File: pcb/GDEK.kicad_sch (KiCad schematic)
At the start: 326 parts, among them J1 TYPE-C-31-M-13C, J101 TYPE-C-31-M-13C, J102 AudioJack4, J103 Debug pads, J2 AudioJack4, J3 Debug pads, SW1 SW_Push_45deg, SW10 SW_Push_45deg, SW101 SW_Push_45deg, SW102 SW_Push_45deg, SW103 SW_Push_45deg, SW104 SW_Push_45deg, SW105 SW_Push_45deg, SW106 SW_Push_45deg, SW107 SW_Push_45deg, SW108 SW_Push_45deg, SW109 SW_Push_45deg, SW11 SW_Push_45deg, SW110 SW_Push_45deg, SW111 SW_Push_45deg, SW112 SW_Push_45deg, SW113 SW_Push_45deg, SW114 SW_Push_45deg, SW115 SW_Push_45deg, SW116 SW_Push_45deg, SW117 SW_Push_45deg, SW118 SW_Push_45deg, SW119 SW_Push_45deg, SW12 SW_Push_45deg, SW120 SW_Push_45deg, SW121 SW_Push_45deg, SW122 SW_Push_45deg, SW123 SW_Push_45deg, SW124 SW_Push_45deg, SW125 SW_Push_45deg, SW126 SW_Push_45deg, SW127 SW_Push_45deg, SW128 SW_Push_45deg, SW129 SW_Push_45deg, SW13 SW_Push_45deg, SW130 SW_Push_45deg, SW131 RotaryEncoder_Switch, SW14 SW_Push_45deg, SW15 SW_Push_45deg, SW16 SW_Push_45deg, SW17 SW_Push_45deg, SW18 SW_Push_45deg, SW19 SW_Push_45deg, SW2 SW_Push_45deg, SW20 SW_Push_45deg, SW21 SW_Push_45deg, SW22 SW_Push_45deg, SW23 SW_Push_45deg, SW24 SW_Push_45deg, SW25 SW_Push_45deg, SW26 SW_Push_45deg, SW27 SW_Push_45deg, SW28 SW_Push_45deg, SW29 SW_Push_45deg, SW3 SW_Push_45deg, SW30 SW_Push_45deg, SW31 RotaryEncoder_Switch, SW4 SW_Push_45deg, SW5 SW_Push_45deg, SW6 SW_Push_45deg, SW7 SW_Push_45deg, SW8 SW_Push_45deg, SW9 SW_Push_45deg, U1 RP2040, U101 RP2040, U102 W25Q128JVS, U103 74AHCT1G125, U104 USBLC6-2P6, U105 XC6210B332MR, U2 W25Q128JVS, U3 74AHCT1G125, U4 USBLC6-2P6, U5 XC6210B332MR, Y1 ABM8-272-T3, Y101 ABM8-272-T3

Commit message: ⚰️ Remove debug pins
YOLO.
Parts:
- removed J103, J3: Debug pads, Connector_PinHeader_2.54mm:PinHeader_1x04_P2.54mm_Vertical, symbol Connector:Conn_01x04_Socket
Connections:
- net ROW1: now also U1.31 (GPIO20); no longer U1.32 (GPIO21)
- net ROW2: now also U1.30 (GPIO19); no longer U1.31 (GPIO20)
- net ROW3: now also U1.29 (GPIO18); no longer U1.30 (GPIO19)
- net ROW4: now also U1.28 (GPIO17); no longer U1.29 (GPIO18)
- net at R102.1: now also U101.32 (GPIO21); no longer U101.41 (GPIO29_ADC3)
- net at R2.1: now also U1.32 (GPIO21); no longer U1.15 (GPIO12)
- no-connect marks 32 -> 36
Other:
- moved on the sheet: C116, C16, R102, R103, R104, R2, R3, R4, TP102, TP2, U102, U2

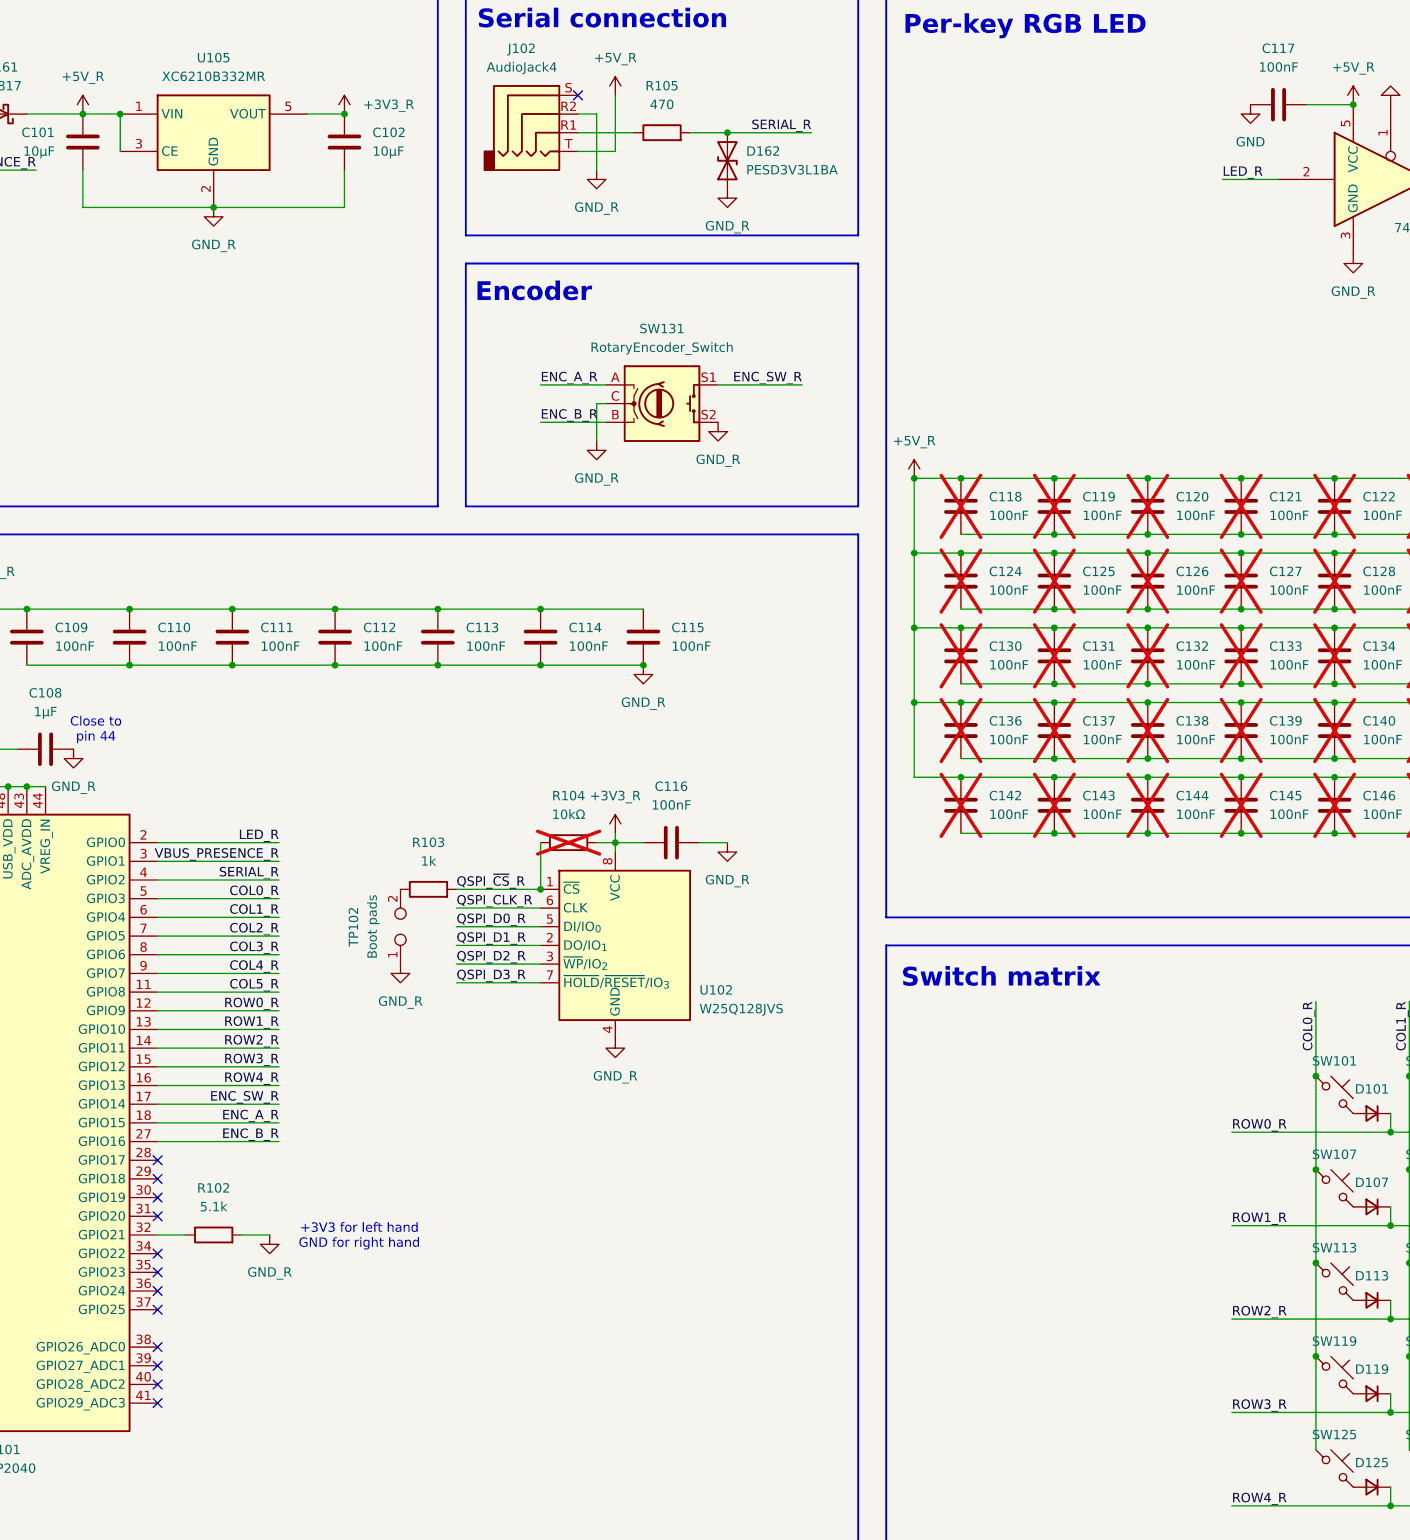
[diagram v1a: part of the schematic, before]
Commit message: ✨ Route right hand (except encoder)
Getting late! Will hopefully finish tomorrow. Then DRC, then panelization with vcuts, then order!
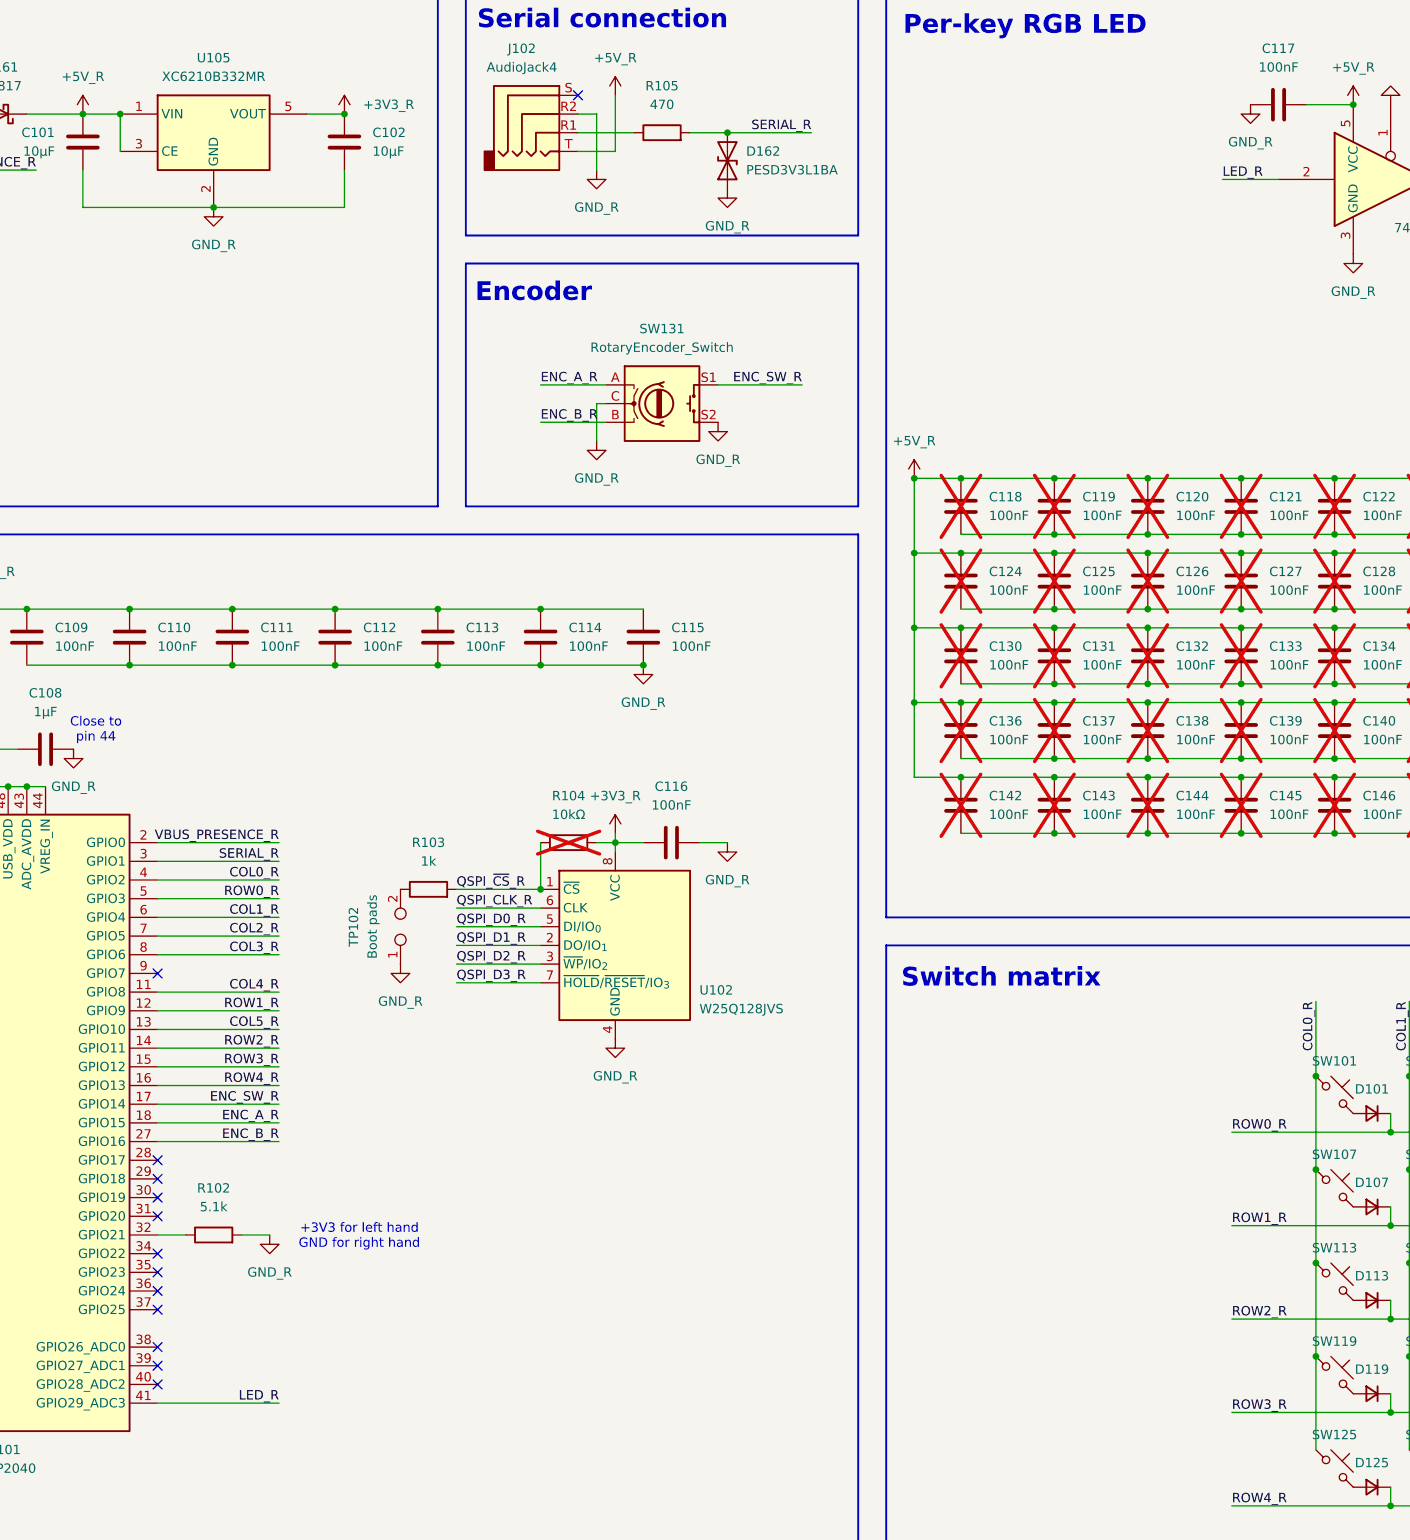
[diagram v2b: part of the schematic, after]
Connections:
- net +3V3_R: now also R104.1; no longer R104.2
- net COL0_R: now also U101.4 (GPIO2); no longer U101.5 (GPIO3)
- net COL4_R: now also U101.11 (GPIO8); no longer U101.9 (GPIO7)
- net COL5_R: now also U101.13 (GPIO10); no longer U101.11 (GPIO8)
- net GND: no longer C117.1
- net GND_R: now also C117.1
- net LED_R: now also U101.41 (GPIO29_ADC3); no longer U101.2 (GPIO0)
- net QSPI_~{CS}_R: now also R104.2; no longer R104.1
- net ROW0_R: now also U101.5 (GPIO3); no longer U101.12 (GPIO9)
- net ROW1_R: now also U101.12 (GPIO9); no longer U101.13 (GPIO10)
- net SERIAL_R: now also U101.3 (GPIO1); no longer U101.4 (GPIO2)
- net VBUS_PRESENCE_R: now also U101.2 (GPIO0); no longer U101.3 (GPIO1)
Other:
- moved on the sheet: R104
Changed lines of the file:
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@@
 	)
 	(no_connect
+		(at 111.76 393.7)
+	)
+	(no_connect
 		(at 60.96 444.5)
 	)
@@
 	)
 	(no_connect
-		(at 111.76 452.12)
-	)
-	(no_connect
 		(at 111.76 142.24)
 	)
@@
 	(wire
 		(pts
-			(xy 128.27 378.46) (xy 111.76 378.46)
+			(xy 128.27 375.92) (xy 111.76 375.92)
 		)
 		(stroke
@@
 	(wire
 		(pts
-			(xy 111.76 393.7) (xy 128.27 393.7)
+			(xy 111.76 396.24) (xy 128.27 396.24)
 		)
 		(stroke
@@
 	(wire
 		(pts
-			(xy 111.76 383.54) (xy 128.27 383.54)
+			(xy 111.76 381) (xy 128.27 381)
 		)
 		(stroke
@@
 	(wire
 		(pts
-			(xy 128.27 381) (xy 111.76 381)
+			(xy 128.27 378.46) (xy 111.76 378.46)
 		)
 		(stroke
@@
 	(wire
 		(pts
-			(xy 111.76 398.78) (xy 128.27 398.78)
+			(xy 111.76 383.54) (xy 128.27 383.54)
 		)
 		(stroke
@@
 	(wire
 		(pts
-			(xy 111.76 401.32) (xy 128.27 401.32)
+			(xy 111.76 398.78) (xy 128.27 398.78)
 		)
 		(stroke
@@
 	(wire
 		(pts
-			(xy 128.27 375.92) (xy 111.76 375.92)
+			(xy 128.27 452.12) (xy 111.76 452.12)
 		)
 		(stroke
@@
 	(wire
 		(pts
-			(xy 111.76 396.24) (xy 128.27 396.24)
+			(xy 111.76 401.32) (xy 128.27 401.32)
 		)
 		(stroke
@@
 	)
 	(label "COL5_R"
-		(at 128.27 396.24 180)
+		(at 128.27 401.32 180)
 		(effects
 			(font
@@
 	)
 	(label "COL4_R"
-		(at 128.27 393.7 180)
+		(at 128.27 396.24 180)
 		(effects
 			(font
@@
 	)
 	(label "LED_R"
-		(at 128.27 375.92 180)
+		(at 128.27 452.12 180)
 		(effects
 			(font
@@
 	)
 	(label "ROW1_R"
-		(at 128.27 401.32 180)
+		(at 128.27 398.78 180)
 		(effects
 			(font
@@
 	)
 	(label "VBUS_PRESENCE_R"
-		(at 128.27 378.46 180)
+		(at 128.27 375.92 180)
 		(effects
 			(font
@@
 	)
 	(label "SERIAL_R"
-		(at 128.27 381 180)
+		(at 128.27 378.46 180)
 		(effects
 			(font
@@
 	)
 	(label "COL0_R"
-		(at 128.27 383.54 180)
+		(at 128.27 381 180)
 		(effects
 			(font
@@
 	)
 	(label "ROW0_R"
-		(at 128.27 398.78 180)
+		(at 128.27 383.54 180)
 		(effects
 			(font
@@
 			)
 		)
-		(property "Value" "GND"
+		(property "Value" "GND_R"
 			(at 260.35 280.67 0)
 			(effects
@@
 	(symbol
 		(lib_id "Device:R")
-		(at 167.64 375.92 90)
+		(at 167.64 375.92 270)
+		(mirror x)
 		(unit 1)
 		(exclude_from_sim no)
@@
 		(on_board yes)
 		(dnp yes)
-		(fields_autoplaced yes)
 		(property "Reference" "R104"
 			(at 167.64 369.57 90)
@@
 		(on_board yes)
 		(dnp no)
-		(fields_autoplaced yes)
 		(property "Reference" "U101"
 			(at 88.5541 458.47 0)

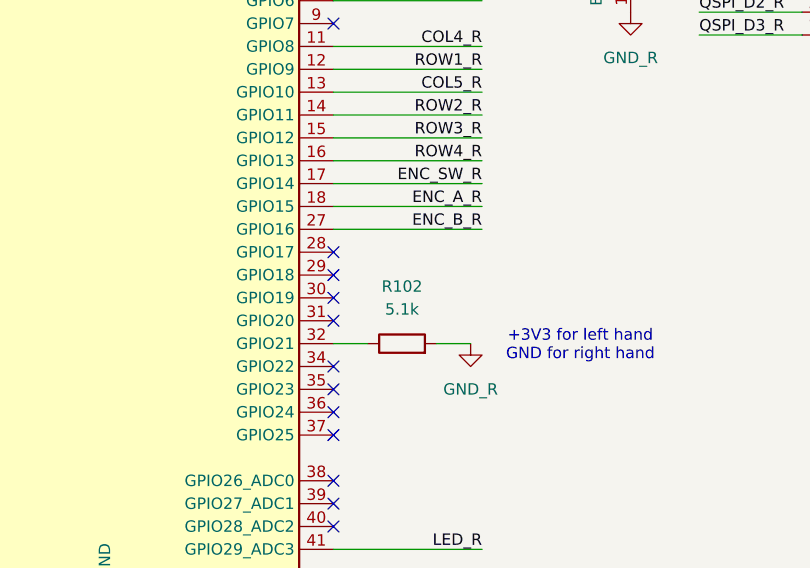
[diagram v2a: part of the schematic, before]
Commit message: ✨ Finish routing of right hand!
Finally! No DRC error!
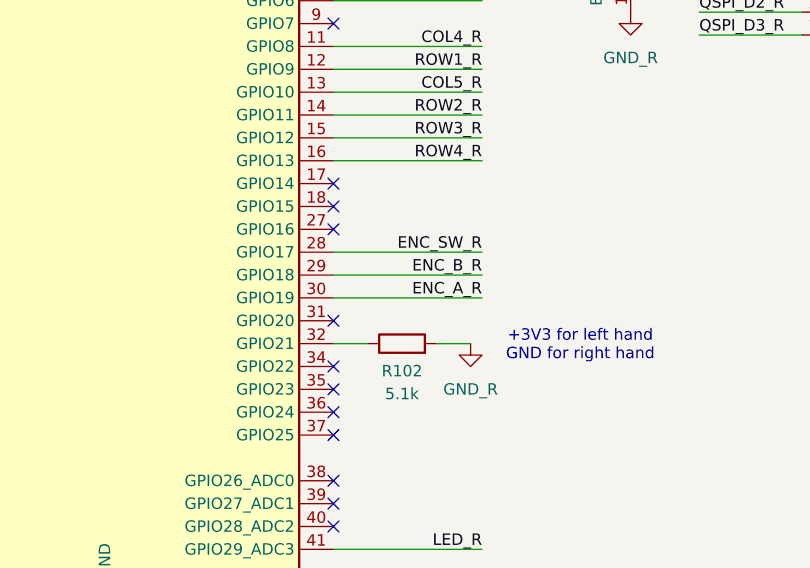
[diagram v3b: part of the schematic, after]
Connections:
- net ENC_A_R: now also U101.30 (GPIO19); no longer U101.18 (GPIO15)
- net ENC_B_R: now also U101.29 (GPIO18); no longer U101.27 (GPIO16)
- net ENC_SW_R: now also U101.28 (GPIO17); no longer U101.17 (GPIO14)
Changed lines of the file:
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@@
 	)
 	(no_connect
+		(at 111.76 416.56)
+	)
+	(no_connect
 		(at 60.96 205.74)
 	)
@@
 	)
 	(no_connect
-		(at 111.76 419.1)
-	)
-	(no_connect
 		(at 111.76 160.02)
 	)
@@
 	)
 	(no_connect
-		(at 111.76 421.64)
-	)
-	(no_connect
 		(at 44.45 66.04)
 	)
@@
 	)
 	(no_connect
+		(at 111.76 414.02)
+	)
+	(no_connect
 		(at 60.96 203.2)
 	)
@@
 	)
 	(no_connect
-		(at 111.76 424.18)
+		(at 44.45 304.8)
 	)
 	(no_connect
-		(at 44.45 304.8)
+		(at 111.76 411.48)
 	)
 	(no_connect
@@
 	(wire
 		(pts
-			(xy 111.76 414.02) (xy 128.27 414.02)
+			(xy 111.76 424.18) (xy 128.27 424.18)
 		)
 		(stroke
@@
 	(wire
 		(pts
-			(xy 111.76 411.48) (xy 128.27 411.48)
+			(xy 111.76 419.1) (xy 128.27 419.1)
 		)
 		(stroke
@@
 	(wire
 		(pts
-			(xy 111.76 416.56) (xy 128.27 416.56)
+			(xy 111.76 421.64) (xy 128.27 421.64)
 		)
 		(stroke
@@
 	)
 	(label "ENC_B_R"
-		(at 128.27 416.56 180)
+		(at 128.27 421.64 180)
 		(effects
 			(font
@@
 	)
 	(label "ENC_A_R"
-		(at 128.27 414.02 180)
+		(at 128.27 424.18 180)
 		(effects
 			(font
@@
 	)
 	(label "ENC_SW_R"
-		(at 128.27 411.48 180)
+		(at 128.27 419.1 180)
 		(effects
 			(font
@@
 		(on_board yes)
 		(dnp no)
-		(fields_autoplaced yes)
 		(property "Reference" "R102"
-			(at 119.38 422.91 90)
+			(at 119.38 432.308 90)
 			(effects
 				(font
@@
 		)
 		(property "Value" "5.1k"
-			(at 119.38 425.45 90)
+			(at 119.38 434.848 90)
 			(effects
 				(font

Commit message: 🎨 Add encoder 3D model
First embedded model, that’s cool!
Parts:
- SW131, SW31: footprint Rotary_Encoder:RotaryEncoder_Alps_EC11E-Switch_Vertical_H20mm -> GDEK:RotaryEncoder_Alps_EC11E-Switch_Vertical_H20mm
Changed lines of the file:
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@@
 			)
 		)
-		(property "Footprint" "Rotary_Encoder:RotaryEncoder_Alps_EC11E-Switch_Vertical_H20mm"
+		(property "Footprint" "GDEK:RotaryEncoder_Alps_EC11E-Switch_Vertical_H20mm"
 			(at 176.53 73.406 0)
 			(effects
@@
 			)
 		)
-		(property "Footprint" "Rotary_Encoder:RotaryEncoder_Alps_EC11E-Switch_Vertical_H20mm"
+		(property "Footprint" "GDEK:RotaryEncoder_Alps_EC11E-Switch_Vertical_H20mm"
 			(at 176.53 312.166 0)
 			(effects
